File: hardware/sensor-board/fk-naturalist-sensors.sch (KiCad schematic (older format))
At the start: 18 parts, among them J1 Conn_01x07, M1 MOUNT_HOLE, M2 MOUNT_HOLE, M3 MOUNT_HOLE, M4 MOUNT_HOLE, U1 MPL3115A2, U2 SHT31, U3 SPH0645, U4 TSL2591

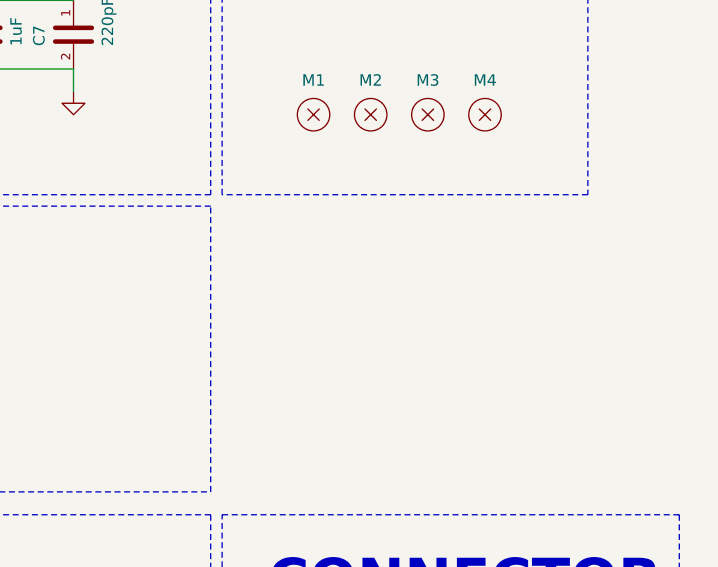
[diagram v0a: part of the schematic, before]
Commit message: Adding fiducials to the sensor board.
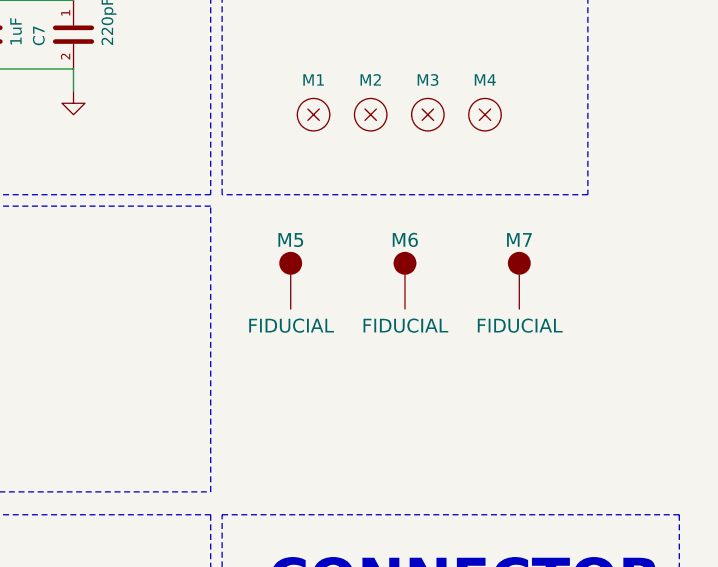
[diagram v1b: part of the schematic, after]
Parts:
- added M5, M6, M7: FIDUCIAL, Fiducials:Fiducial_0.75mm_Dia_1.5mm_Outer, symbol FIDUCIAL
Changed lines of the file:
@@
 LIBS:contrib
 LIBS:valves
-LIBS:conservify
+LIBS:RocketScreamKicadLibrary
 LIBS:fk-naturalist-sensors-cache
 EELAYER 25 0
@@
 Wire Notes Line
 	6900 5100 6900 3400
+$Comp
+L FIDUCIAL M5
+U 1 1 5B243ED0
+P 7200 2350
+F 0 "M5" H 7200 2500 60  0000 C CNN
+F 1 "FIDUCIAL" H 7200 2125 60  0000 C CNN
+F 2 "Fiducials:Fiducial_0.75mm_Dia_1.5mm_Outer" H 7200 2050 60  0001 C CNN
+F 3 "" H 7200 2350 60  0000 C CNN
+	1    7200 2350
+	1    0    0    -1
+$EndComp
+$Comp
+L FIDUCIAL M6
+U 1 1 5B243F25
+P 7700 2350
+F 0 "M6" H 7700 2500 60  0000 C CNN
+F 1 "FIDUCIAL" H 7700 2125 60  0000 C CNN
+F 2 "Fiducials:Fiducial_0.75mm_Dia_1.5mm_Outer" H 7700 2050 60  0001 C CNN
+F 3 "" H 7700 2350 60  0000 C CNN
+	1    7700 2350
+	1    0    0    -1
+$EndComp
+$Comp
+L FIDUCIAL M7
+U 1 1 5B243F74
+P 8200 2350
+F 0 "M7" H 8200 2500 60  0000 C CNN
+F 1 "FIDUCIAL" H 8200 2125 60  0000 C CNN
+F 2 "Fiducials:Fiducial_0.75mm_Dia_1.5mm_Outer" H 8200 2050 60  0001 C CNN
+F 3 "" H 8200 2350 60  0000 C CNN
+	1    8200 2350
+	1    0    0    -1
+$EndComp
 $EndSCHEMATC

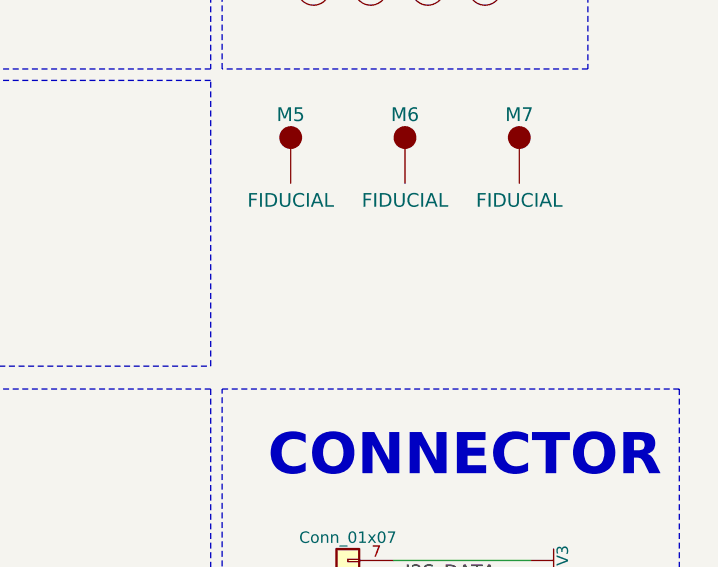
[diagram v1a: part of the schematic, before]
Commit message: Adding fiducials to the bottom.
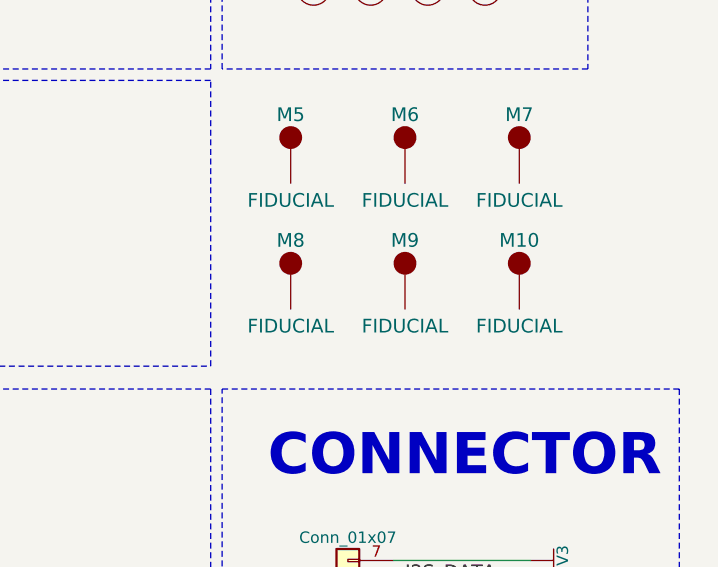
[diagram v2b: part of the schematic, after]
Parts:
- added M10, M8, M9: FIDUCIAL, Fiducials:Fiducial_0.75mm_Dia_1.5mm_Outer, symbol FIDUCIAL
- M1, M2, M3, M4: footprint RocketScreamKicadLibrary:HOLE_PTH_3.2MM -> conservify:HOLE_NPTH_3.2MM
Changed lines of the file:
@@
 F 0 "M1" H 7300 1800 50  0000 C CNN
 F 1 "MOUNT_HOLE" H 7300 1500 50  0001 C CNN
-F 2 "RocketScreamKicadLibrary:HOLE_PTH_3.2MM" H 7325 1425 50  0001 C CNN
+F 2 "conservify:HOLE_NPTH_3.2MM" H 7325 1425 50  0001 C CNN
 F 3 "" H 7300 1650 50  0000 C CNN
 	1    7300 1650
@@
 F 0 "M2" H 7550 1800 50  0000 C CNN
 F 1 "MOUNT_HOLE" H 7550 1500 50  0001 C CNN
-F 2 "RocketScreamKicadLibrary:HOLE_PTH_3.2MM" H 7575 1425 50  0001 C CNN
+F 2 "conservify:HOLE_NPTH_3.2MM" H 7575 1425 50  0001 C CNN
 F 3 "" H 7550 1650 50  0000 C CNN
 	1    7550 1650
@@
 F 0 "M3" H 7800 1800 50  0000 C CNN
 F 1 "MOUNT_HOLE" H 7800 1500 50  0001 C CNN
-F 2 "RocketScreamKicadLibrary:HOLE_PTH_3.2MM" H 7825 1425 50  0001 C CNN
+F 2 "conservify:HOLE_NPTH_3.2MM" H 7825 1425 50  0001 C CNN
 F 3 "" H 7800 1650 50  0000 C CNN
 	1    7800 1650
@@
 F 0 "M4" H 8050 1800 50  0000 C CNN
 F 1 "MOUNT_HOLE" H 8050 1500 50  0001 C CNN
-F 2 "RocketScreamKicadLibrary:HOLE_PTH_3.2MM" H 8075 1425 50  0001 C CNN
+F 2 "conservify:HOLE_NPTH_3.2MM" H 8075 1425 50  0001 C CNN
 F 3 "" H 8050 1650 50  0000 C CNN
 	1    8050 1650
@@
 	1    0    0    -1
 $EndComp
+$Comp
+L FIDUCIAL M8
+U 1 1 5B33D073
+P 7200 2900
+F 0 "M8" H 7200 3050 60  0000 C CNN
+F 1 "FIDUCIAL" H 7200 2675 60  0000 C CNN
+F 2 "Fiducials:Fiducial_0.75mm_Dia_1.5mm_Outer" H 7200 2600 60  0001 C CNN
+F 3 "" H 7200 2900 60  0000 C CNN
+	1    7200 2900
+	1    0    0    -1
+$EndComp
+$Comp
+L FIDUCIAL M9
+U 1 1 5B33D079
+P 7700 2900
+F 0 "M9" H 7700 3050 60  0000 C CNN
+F 1 "FIDUCIAL" H 7700 2675 60  0000 C CNN
+F 2 "Fiducials:Fiducial_0.75mm_Dia_1.5mm_Outer" H 7700 2600 60  0001 C CNN
+F 3 "" H 7700 2900 60  0000 C CNN
+	1    7700 2900
+	1    0    0    -1
+$EndComp
+$Comp
+L FIDUCIAL M10
+U 1 1 5B33D07F
+P 8200 2900
+F 0 "M10" H 8200 3050 60  0000 C CNN
+F 1 "FIDUCIAL" H 8200 2675 60  0000 C CNN
+F 2 "Fiducials:Fiducial_0.75mm_Dia_1.5mm_Outer" H 8200 2600 60  0001 C CNN
+F 3 "" H 8200 2900 60  0000 C CNN
+	1    8200 2900
+	1    0    0    -1
+$EndComp
